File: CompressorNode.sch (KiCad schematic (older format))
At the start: 34 parts, among them J1 EXT1, J10 Screw_Terminal_01x03, J11 Screw_Terminal_01x02, J12 Screw_Terminal_01x03, J13 Screw_Terminal_01x04, J2 Screw_Terminal_01x04, J3 Screw_Terminal_01x03, J4 EXT2, J5 Screw_Terminal_01x02, J6 Screw_Terminal_01x02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

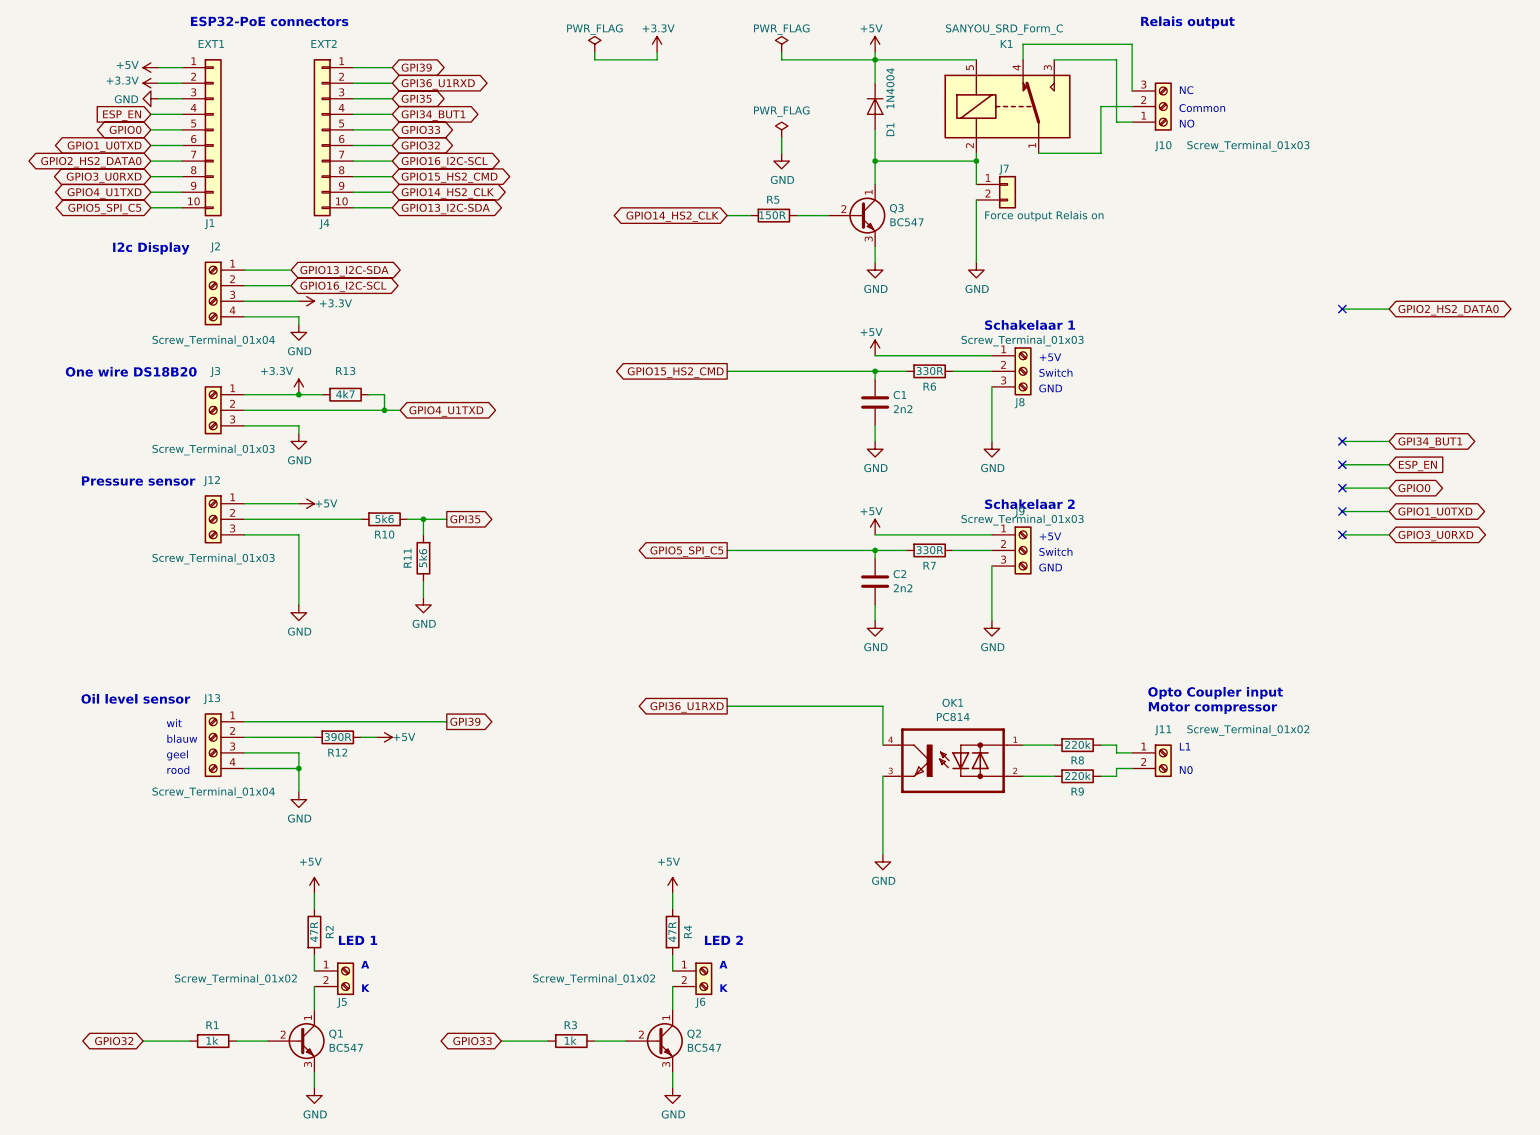
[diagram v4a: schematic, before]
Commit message: V0.16 concept: LED in switches are switched on or off to show which one can be pressed
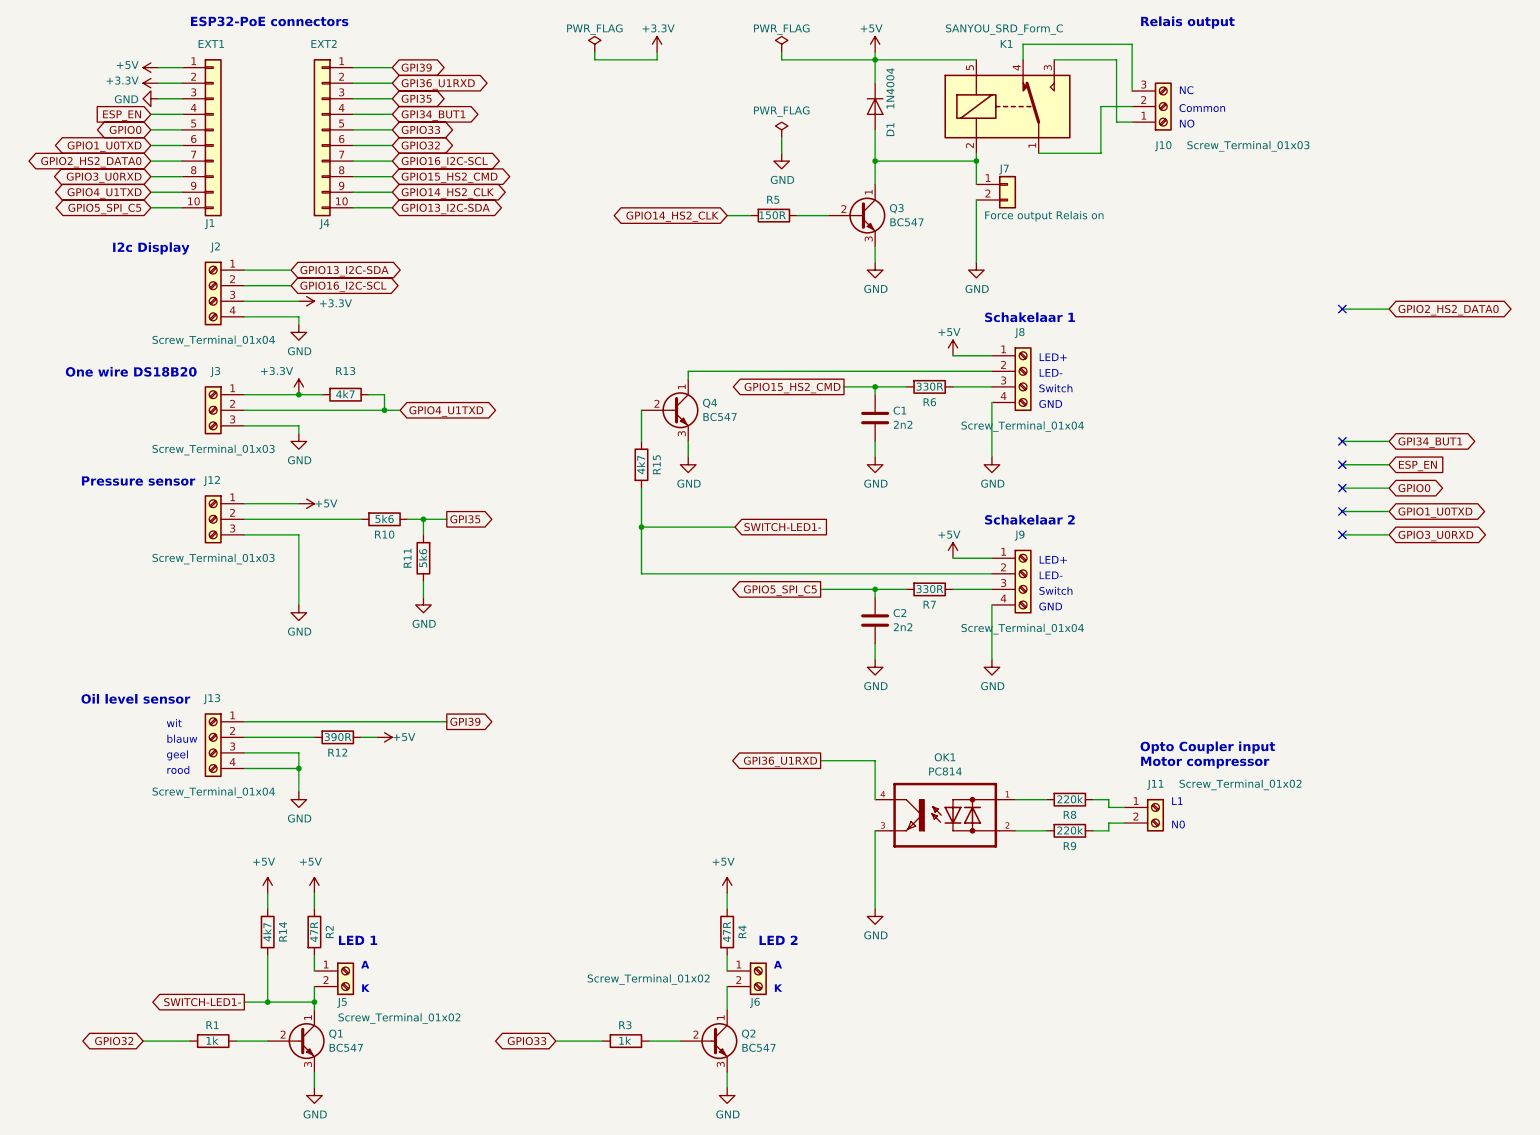
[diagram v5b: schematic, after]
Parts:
- removed J8, J9: Screw_Terminal_01x03, TerminalBlock_RND:TerminalBlock_RND_205-00288_1x03_P5.08mm_Horizontal, symbol Connector:Screw_Terminal_01x03
- added J8, J9: Screw_Terminal_01x04, TerminalBlock_RND:TerminalBlock_RND_205-00289_1x04_P5.08mm_Horizontal, symbol Connector:Screw_Terminal_01x04
- added Q4: BC547, Package_TO_SOT_THT:TO-92_Inline, symbol Transistor_BJT:BC547
- added R14, R15: 4k7, Resistor_THT:R_Axial_DIN0207_L6.3mm_D2.5mm_P7.62mm_Horizontal, symbol Device:R
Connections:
- net +5V: now also J8.1 (Pin_1), J9.1 (Pin_1), R14.1
- net GND: now also J8.4 (Pin_4), J9.4 (Pin_4), Q4.3 (E)
- net SWITCH-LED1-: now reaches J5.2 (Pin_2), Q1.1 (C)
- net SWITCH-LED1-: now also J9.2 (Pin_2), R14.2, R15.2
- net at R7.1: now also J9.3 (Pin_3)
- net at R6.1: now also J8.3 (Pin_3)
- new net: J8.2 (Pin_2), Q4.1 (C)
- new net: Q4.2 (B), R15.1
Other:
- note added: "LED+"
- note added: "LED-"
- note removed: "+5V"
- moved on the sheet: C1, C2, J11, J6, OK1, Q2, R3, R4, R6, R7, R8, R9

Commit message: Changed some labels and R15 chanched to 47k V0.18
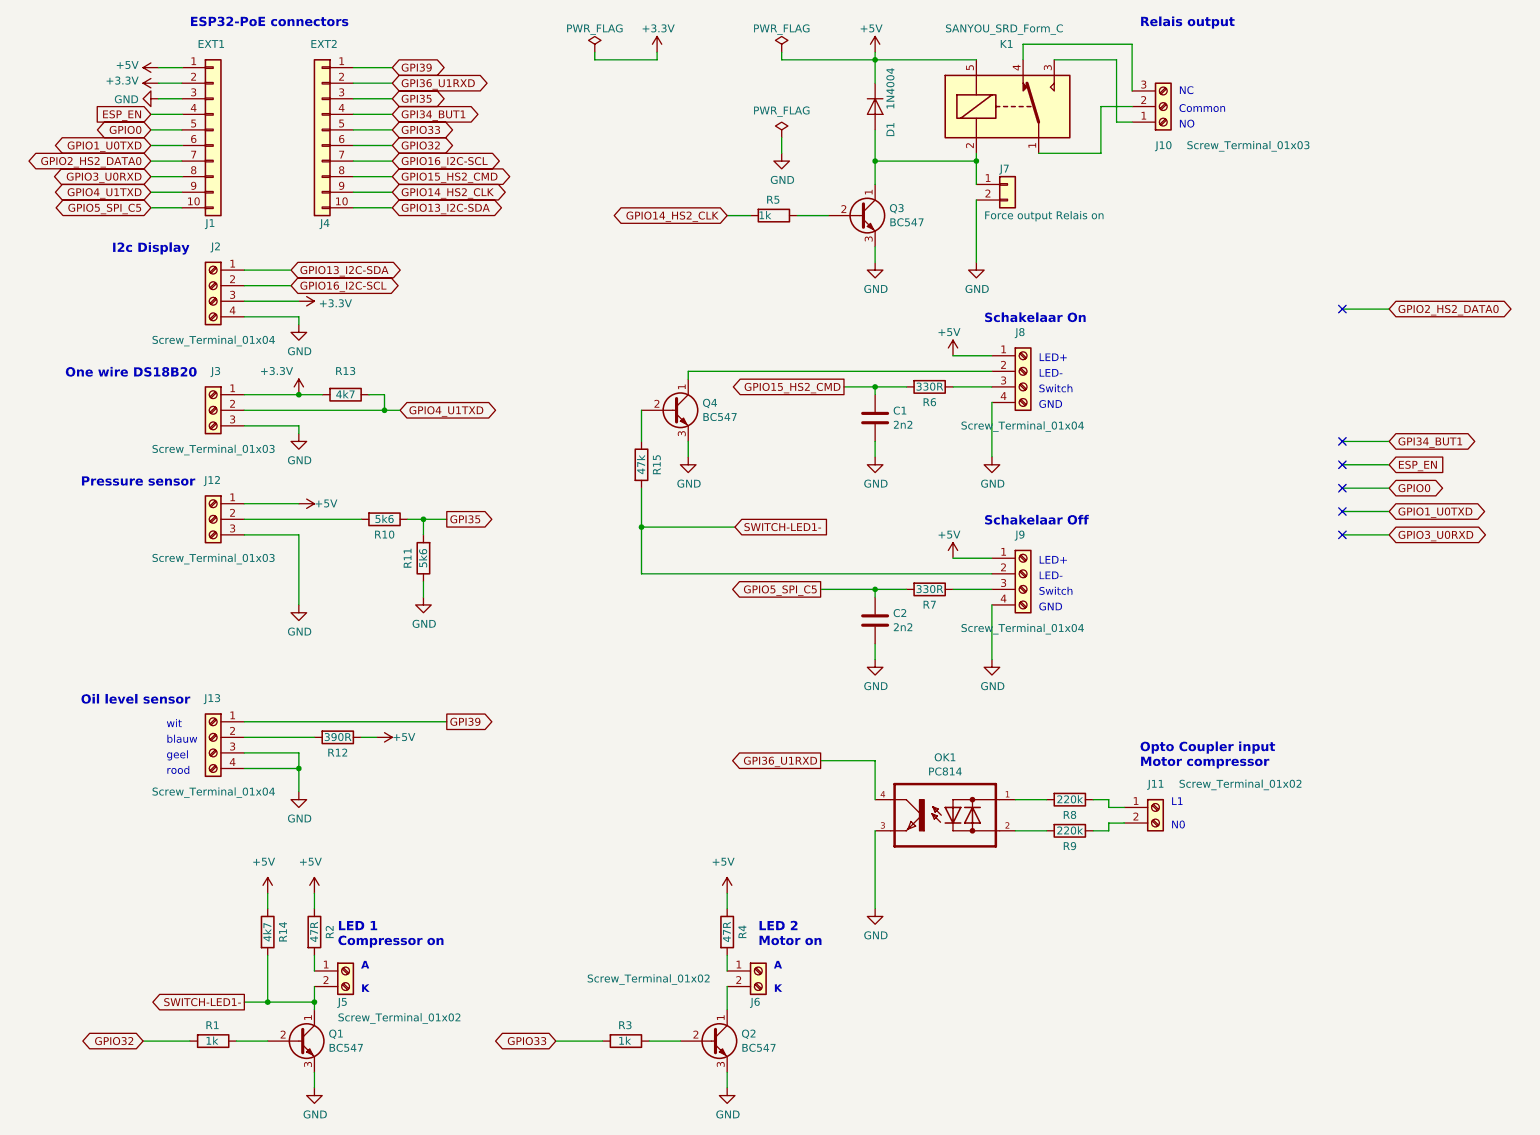
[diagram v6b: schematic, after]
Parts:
- R15: value 4k7 -> 47k
- R5: value 150R -> 1k
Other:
- note added: "LED 1\nCompressor on"
- note added: "LED 2\nMotor on"
- note added: "Schakelaar Off"
- note added: "Schakelaar On"
- note removed: "LED 1"
- note removed: "LED 2"
- note removed: "Schakelaar 1"
- note removed: "Schakelaar 2"
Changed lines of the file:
@@
 Sheet 1 1
 Title "CompressorNode"
-Date "2020-04-20"
-Rev "V0.16 Concept"
+Date "2020-04-27"
+Rev "V0.17 Concept"
 Comp "MakerSpace Leiden"
 Comment1 "Getekend door Hans Beerman"
@@
 GPI36_U1RXD
 Text Notes 7050 2600 0    59   ~ 12
-Schakelaar 1
+Schakelaar On
 $Comp
 L power:GND #PWR020
@@
 P 5700 1900
 F 0 "R5" V 5600 1850 50  0000 L CNN
-F 1 "150R" V 5700 1800 50  0000 L CNN
+F 1 "1k" V 5700 1800 50  0000 L CNN
 F 2 "Resistor_THT:R_Axial_DIN0207_L6.3mm_D2.5mm_P7.62mm_Horizontal" V 5630 1900 50  0001 C CNN
 F 3 "~" H 5700 1900 50  0001 C CNN
@@
 	6350 4300 6550 4300
 Text Notes 7050 3900 0    59   ~ 12
-Schakelaar 2
+Schakelaar Off
 $Comp
 L power:GND #PWR021
@@
 	5400 6350 5400 6250
 Text Notes 2900 6600 0    59   ~ 12
-LED 1
+LED 1\nCompressor on
 Text Notes 5600 6600 0    59   ~ 12
-LED 2
+LED 2\nMotor on
 Text GLabel 2600 2250 2    50   BiDi ~ 0
 GPIO13_I2C-SDA
@@
 P 4850 3500
 F 0 "R15" V 4950 3500 50  0000 C CNN
-F 1 "4k7" V 4850 3500 50  0000 C CNN
+F 1 "47k" V 4850 3500 50  0000 C CNN
 F 2 "Resistor_THT:R_Axial_DIN0207_L6.3mm_D2.5mm_P7.62mm_Horizontal" V 4780 3500 50  0001 C CNN
 F 3 "~" H 4850 3500 50  0001 C CNN

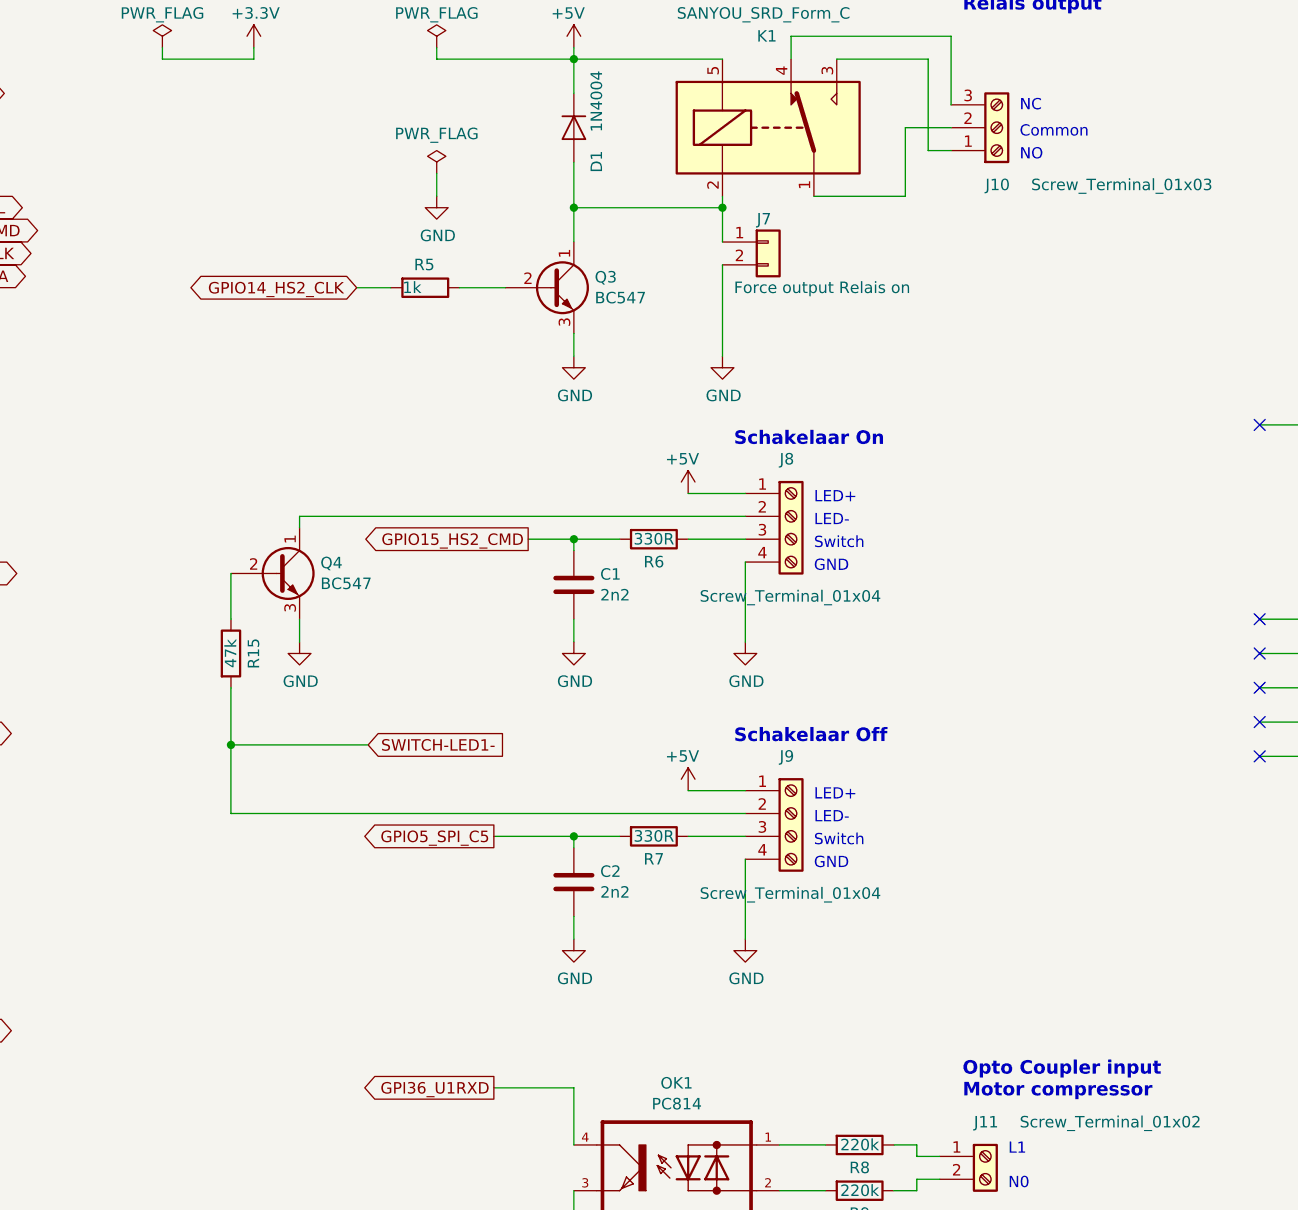
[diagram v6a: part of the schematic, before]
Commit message: V0.18: added a screw connector for safety, to switch of compressor in case a cable is disconnected
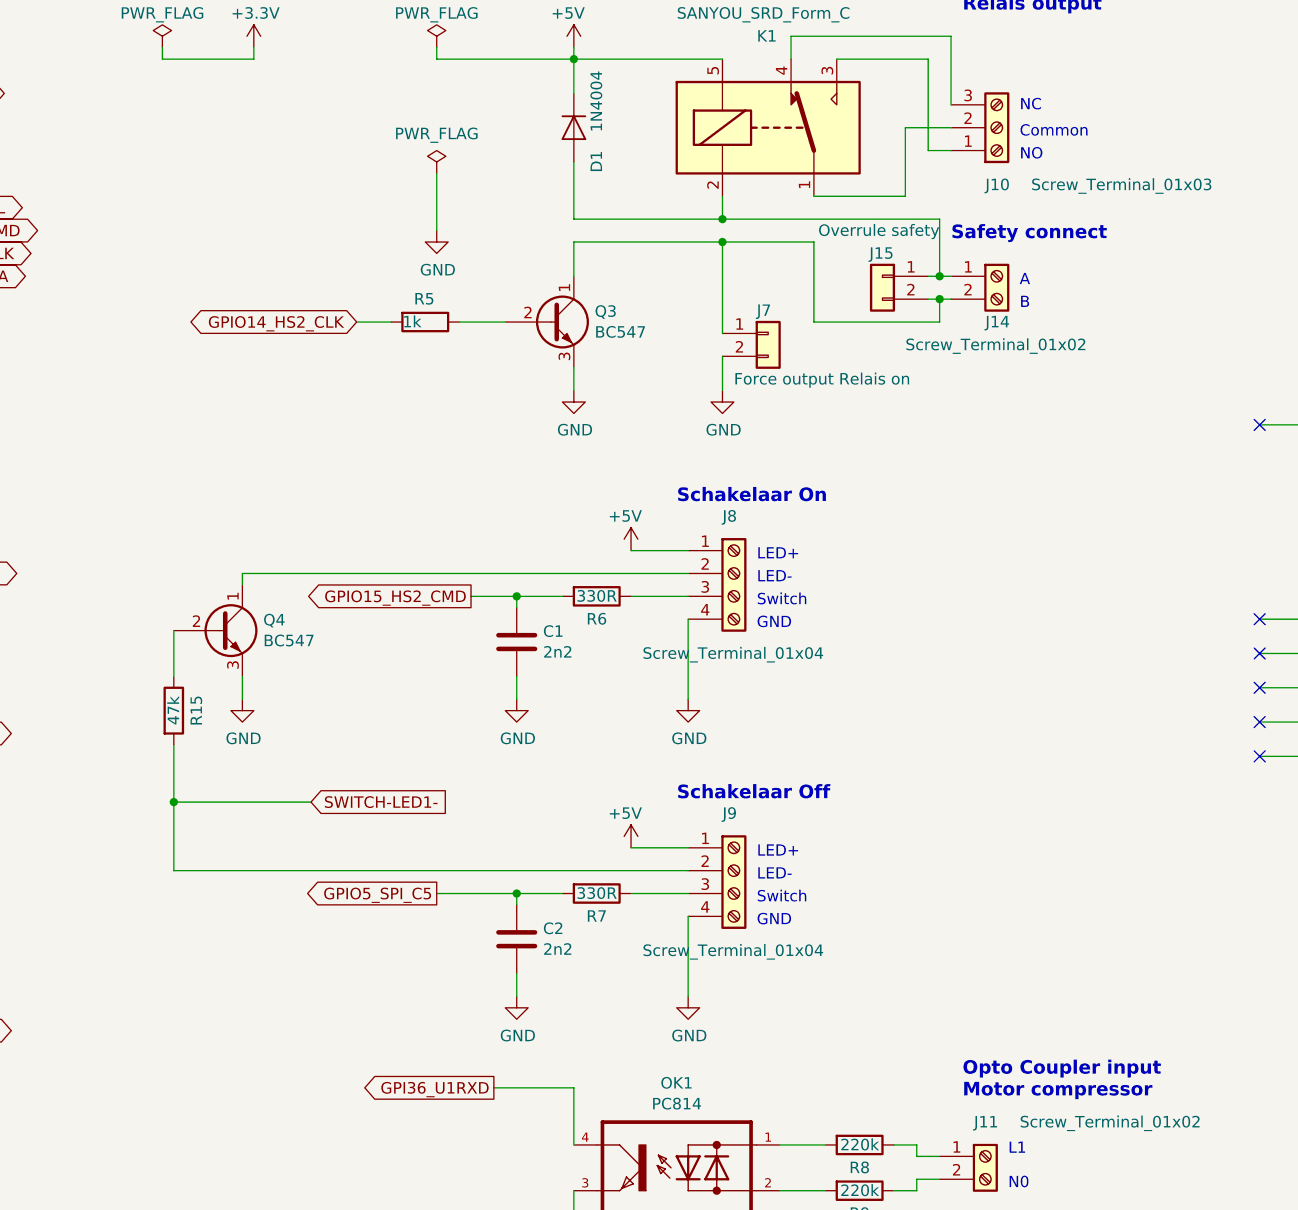
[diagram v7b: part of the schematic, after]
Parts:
- added J14: Screw_Terminal_01x02, TerminalBlock_RND:TerminalBlock_RND_205-00287_1x02_P5.08mm_Horizontal, symbol Connector:Screw_Terminal_01x02
- added J15: Overrule safety, Connector_PinHeader_2.54mm:PinHeader_1x02_P2.54mm_Vertical, symbol Connector_Generic:Conn_01x02
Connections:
- net at J7.1 (Pin_1), Q3.1 (C): now also J14.2 (Pin_2), J15.2 (Pin_2); no longer D1.2 (A), K1.2
- new net: D1.2 (A), J14.1 (Pin_1), J15.1 (Pin_1), K1.2
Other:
- note added: "B"
- note added: "Safety connect"
- moved on the sheet: C1, C2, J7, J8, J9, Q3, Q4, R15, R5, R6, R7
